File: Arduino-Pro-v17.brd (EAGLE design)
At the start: 37.8 x 53.3 mm, 38 parts, among them IC1 ATMEGA1281-16AU, IC2 MCP170312MB, J1 FTDI Basic Programmer

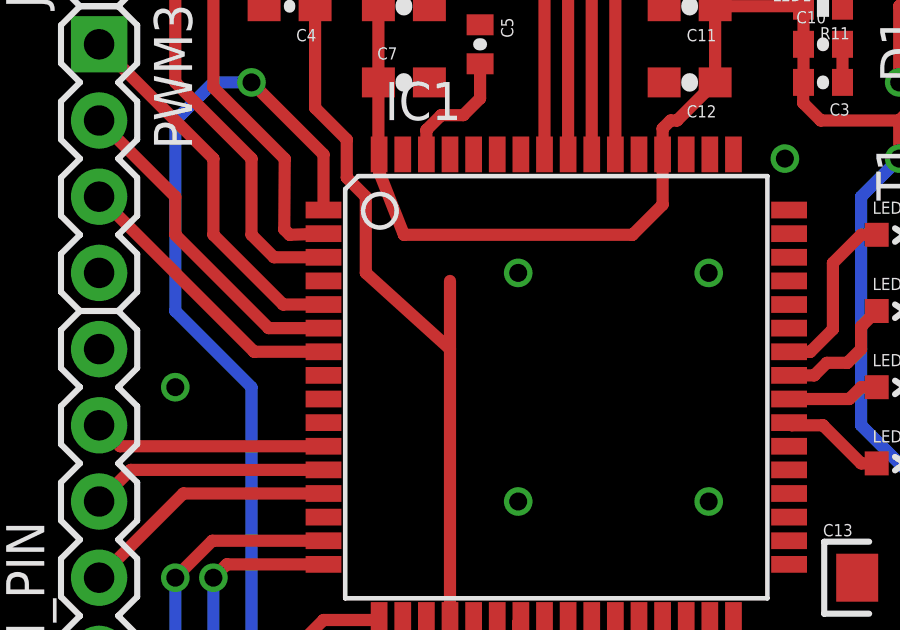
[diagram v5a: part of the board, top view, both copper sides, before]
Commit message: Fixed stray route under atmel chip
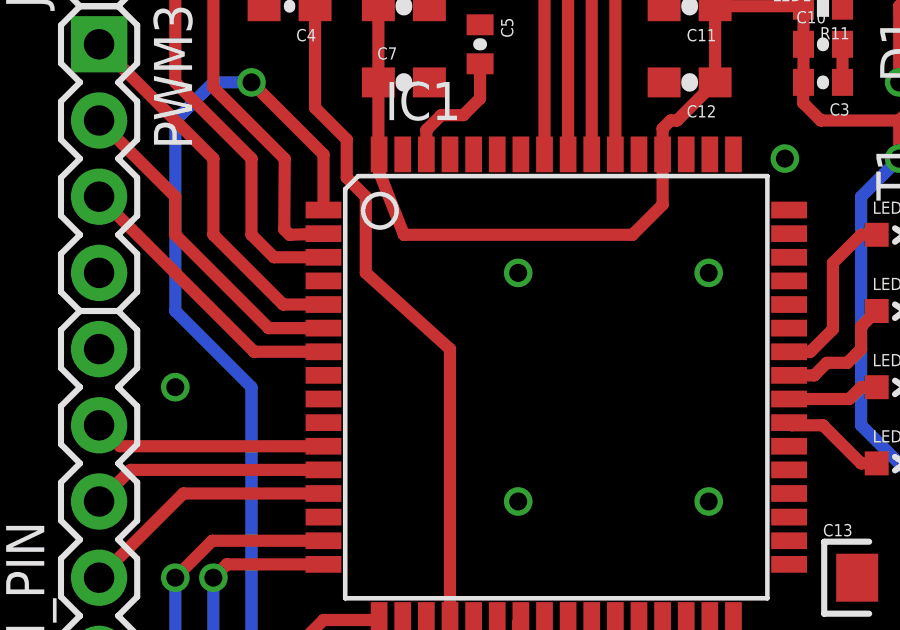
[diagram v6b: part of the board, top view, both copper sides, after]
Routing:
- net RESET: track 34.1 -> 31.8 mm
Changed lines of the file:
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@@
 <wire x1="19.05" y1="63.51" x2="21.17" y2="61.39" width="0.4064" layer="1"/>
 <wire x1="25.6667" y1="37.9603" x2="25.6667" y2="46.99" width="0.4064" layer="1"/>
-<wire x1="25.6667" y1="46.99" x2="25.6667" y2="49.2633" width="0.4064" layer="1"/>
 <wire x1="21.17" y1="58.42" x2="21.17" y2="55.03" width="0.4064" layer="1"/>
 <wire x1="21.17" y1="55.03" x2="22.225" y2="53.975" width="0.4064" layer="1"/>

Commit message: Fixed some things with the board layout
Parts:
- added D2: 3.3V, SparkFun-DiscreteSemi:SOD-323
- J2: device SparkFun-Connectors:1X02 -> SparkFun-Connectors:1X03
- moved LED1 20.1 mm to (43.2, 40.6)
- moved C3 19.7 mm to (43.2, 36.8)
- moved R11 19.7 mm to (43.2, 39.4)
- moved C10 19.7 mm to (43.2, 38.1)
- moved C13 18.2 mm to (36.8, 57.1), turned to 270 degrees
- moved T1 5.39 mm to (40.6, 57.1), turned to 270 degrees
- moved C2 4.84 mm to (24.9, 25.5)
- moved Y1 4.47 mm to (28.3, 29.1)
- moved C1 3.83 mm to (31.7, 25.6)
- moved LED2 3.81 mm to (40.6, 47.0)
- moved R5 3.81 mm to (44.5, 47.0)
- moved C8 2.54 mm to (25.4, 35.6)
- moved C9 2.54 mm to (25.4, 33.0)
- moved I2C_PIN 2.54 mm to (36.8, 34.3)
- moved LED3 2.54 mm to (40.6, 45.7)
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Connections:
- net 5VROV: now also J2.3; no longer J2.2
- net ALTVCC: now also D2.C
- net GND: now also D2.A, J2.2
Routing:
- net VCC: track 99.4 -> 115.7 mm, vias 3 -> 5
- net ALTVCC: track 14.1 -> 6.72 mm, vias 1 -> 0
- net PWM0B: track 39.4 -> 33.7 mm, vias 1 -> 0
- net N$3: track 9.14 -> 13.5 mm
- net PWM0A: track 16.7 -> 13.0 mm
- net N$11: track 5.83 -> 2.96 mm
- net 3V3: track 50.9 -> 53.8 mm, vias 3 -> 1
- net SCL: track 15.0 -> 12.5 mm
- net 5VROV: track 4.14 -> 6.13 mm
- net SDA: track 12.2 -> 10.4 mm
- net N$1: track 11.5 -> 13.2 mm
- net PWM1B: track 13.1 -> 11.6 mm, vias 1 -> 0
- net PWM1A: track 11.6 -> 10.1 mm, vias 1 -> 0
- net GND: track 1.27 -> 0.00 mm
- net N$10: track 4.25 -> 3.08 mm
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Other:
- board size 37.8 x 53.3 mm -> 39 x 53.3 mm

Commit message: Complete final changes
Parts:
- moved C3 16.7 mm to (40.6, 53.3), turned to 0 degrees
- moved C10 14.2 mm to (40.6, 52.1), turned to 180 degrees
- moved R11 11.7 mm to (40.6, 50.8), turned to 0 degrees
- moved LED1 9.07 mm to (40.7, 49.4), turned to 270 degrees
- moved T1 8.13 mm to (45.7, 50.8), turned to 0 degrees
- moved C13 2.54 mm to (39.4, 57.1)
- moved D2 1.27 mm to (41.3, 61.0)
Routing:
- net ALTVCC: track 6.72 -> 18.8 mm, vias 0 -> 2
- net VCC: track 115.7 -> 111.0 mm, vias 5 -> 4
- net 3V3: track 53.8 -> 51.5 mm
- net PWM0B: track 33.7 -> 32.7 mm
